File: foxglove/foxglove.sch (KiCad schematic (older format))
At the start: 87 parts, among them IC1 LFE5U-12F-6BG256C, J1 NEIGHBOR1, J2 NEIGHBOR2, J3 Conn_02x05_Odd_Even, J4 Conn_02x05_Odd_Even, J5 Conn_01x02_Female, J6 Conn_02x03_Odd_Even, J7 BONUS_ROW, U1 LM393, U2 ADP225, U25 74LVC1G53, U3 AP2127, U4 74LVC1G3157, U5 AP2127, U6 AP2127, U7 DAC084S085

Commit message: Routed ADC/DAC and FPGA passives
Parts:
- removed C17: 100nF, gsg-modules:0402, symbol Device:C
- removed C20: 10nF, gsg-modules:0402, symbol Device:C
- added TP1, TP2: TestPoint, gsg-modules:TESTPOINT-50MIL, symbol Connector:TestPoint
- U2: footprint Package_CSP:LFCSP-8_2x2mm_P0.5mm -> gsg-modules:SON50P200X200X60-9N
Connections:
- net +1V1: now also U2.7 (VOUT1), TP2.1
- net +2V5: now also U2.5 (VOUT2), TP1.1
- net +5V: now also U2.1 (EN1), U2.2 (EN2), U2.6 (VIN)
- net CSSPIN: now also J1.24 (Pin_24)
- net GND: now also U2.0 (EPAD)
- net VCC: no longer IC1.F6 (VCCIO0_1), IC1.F7 (VCCIO0_2)
- net at U2.4 (ADJ2): now also R41.1, R42.2
- net at U2.8 (ADJ1): now also R43.2, R44.1
- net J1.24: no longer names the net of IC1.R7 (PB6A)
- net J1.24: no longer J1.24 (Pin_24)
- new net VCCIO0: IC1.F6 (VCCIO0_1), IC1.F7 (VCCIO0_2)
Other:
- moved on the sheet: R41, R42, U2
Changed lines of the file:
@@
 Text Label -11900 8300 1    50   ~ 0
 J1.22
-Text Label -11800 8300 1    50   ~ 0
-J1.24
 Text Label -11700 8300 1    50   ~ 0
 J1.26
@@
 L gsg-symbols:ADP225 U2
 U 1 1 5CCD2B79
-P 10300 1600
-F 0 "U2" H 10275 1975 50  0000 C CNN
-F 1 "ADP225" H 10275 1884 50  0000 C CNN
-F 2 "Package_CSP:LFCSP-8_2x2mm_P0.5mm" H 10150 1600 50  0001 C CNN
-F 3 "" H 10150 1600 50  0001 C CNN
-F 4 "Analog Devices Inc. " H 10300 1600 50  0001 C CNN "Manufacturer"
-F 5 "ADP225ACPZ-R7" H 10300 1600 50  0001 C CNN "Part Number"
-F 6 "IC REG LINEAR POS ADJ 8LFCSP" H 10300 1600 50  0001 C CNN "Description"
-	1    10300 1600
+P 10200 1600
+F 0 "U2" H 10175 1975 50  0000 C CNN
+F 1 "ADP225" H 10175 1884 50  0000 C CNN
+F 2 "gsg-modules:SON50P200X200X60-9N" H 10050 1600 50  0001 C CNN
+F 3 "" H 10050 1600 50  0001 C CNN
+F 4 "Analog Devices Inc. " H 10200 1600 50  0001 C CNN "Manufacturer"
+F 5 "ADP225ACPZ-R7" H 10200 1600 50  0001 C CNN "Part Number"
+F 6 "IC REG LINEAR POS ADJ 8LFCSP" H 10200 1600 50  0001 C CNN "Description"
+	1    10200 1600
 	1    0    0    -1
 $EndComp
@@
 L power:GND #PWR0200
 U 1 1 5CD3745C
-P 9850 1650
-F 0 "#PWR0200" H 9850 1400 50  0001 C CNN
-F 1 "GND" H 9850 1500 50  0000 C CNN
-F 2 "" H 9850 1650 50  0001 C CNN
-F 3 "" H 9850 1650 50  0001 C CNN
-	1    9850 1650
+P 9700 1650
+F 0 "#PWR0200" H 9700 1400 50  0001 C CNN
+F 1 "GND" H 9700 1500 50  0000 C CNN
+F 2 "" H 9700 1650 50  0001 C CNN
+F 3 "" H 9700 1650 50  0001 C CNN
+	1    9700 1650
 	0    1    1    0
 $EndComp
 Wire Wire Line
-	9850 1650 9900 1650
-Wire Wire Line
 	10650 1650 11150 1650
 Wire Wire Line
@@
 L Device:R R42
 U 1 1 5CF1DBFB
-P 10250 1900
-F 0 "R42" V 10457 1900 50  0000 C CNN
-F 1 "100k" V 10366 1900 50  0000 C CNN
-F 2 "gsg-modules:0402" V 10180 1900 50  0001 C CNN
-F 3 "~" H 10250 1900 50  0001 C CNN
-	1    10250 1900
+P 10250 2000
+F 0 "R42" V 10457 2000 50  0000 C CNN
+F 1 "100k" V 10366 2000 50  0000 C CNN
+F 2 "gsg-modules:0402" V 10180 2000 50  0001 C CNN
+F 3 "~" H 10250 2000 50  0001 C CNN
+	1    10250 2000
 	0    1    1    0
 $EndComp
 Wire Wire Line
-	9900 1750 9900 1900
-Wire Wire Line
-	9900 1900 10100 1900
-Wire Wire Line
 	10650 1750 10700 1750
-Wire Wire Line
-	10400 1900 10700 1900
-Wire Wire Line
-	10700 1900 10700 1750
 $Comp
 L power:+2V5 #PWR0205
@@
 L Device:R R41
 U 1 1 5CFF97C1
-P 9700 1900
-F 0 "R41" V 9907 1900 50  0000 C CNN
-F 1 "25k" V 9816 1900 50  0000 C CNN
-F 2 "gsg-modules:0402" V 9630 1900 50  0001 C CNN
-F 3 "~" H 9700 1900 50  0001 C CNN
-	1    9700 1900
+P 9550 1900
+F 0 "R41" V 9757 1900 50  0000 C CNN
+F 1 "25k" V 9666 1900 50  0000 C CNN
+F 2 "gsg-modules:0402" V 9480 1900 50  0001 C CNN
+F 3 "~" H 9550 1900 50  0001 C CNN
+	1    9550 1900
 	0    1    1    0
 $EndComp
-Wire Wire Line
-	9850 1900 9900 1900
-Connection ~ 9900 1900
 $Comp
 L power:GND #PWR0207
 U 1 1 5D01F043
-P 9500 1900
-F 0 "#PWR0207" H 9500 1650 50  0001 C CNN
-F 1 "GND" H 9500 1750 50  0000 C CNN
-F 2 "" H 9500 1900 50  0001 C CNN
-F 3 "" H 9500 1900 50  0001 C CNN
-	1    9500 1900
+P 9350 1900
+F 0 "#PWR0207" H 9350 1650 50  0001 C CNN
+F 1 "GND" H 9350 1750 50  0000 C CNN
+F 2 "" H 9350 1900 50  0001 C CNN
+F 3 "" H 9350 1900 50  0001 C CNN
+	1    9350 1900
 	0    1    1    0
 $EndComp
 Wire Wire Line
-	9500 1900 9550 1900
-Wire Wire Line
-	9900 1550 9900 1500
-Wire Wire Line
-	9900 1500 9850 1500
-Connection ~ 9900 1500
-Wire Wire Line
-	9900 1500 9900 1450
+	9350 1900 9400 1900
 $Comp
 L power:+5V #PWR0208
 U 1 1 5D091620
-P 9850 1500
-F 0 "#PWR0208" H 9850 1350 50  0001 C CNN
-F 1 "+5V" H 9865 1673 50  0000 C CNN
-F 2 "" H 9850 1500 50  0001 C CNN
-F 3 "" H 9850 1500 50  0001 C CNN
-	1    9850 1500
+P 9700 1500
+F 0 "#PWR0208" H 9700 1350 50  0001 C CNN
+F 1 "+5V" H 9715 1673 50  0000 C CNN
+F 2 "" H 9700 1500 50  0001 C CNN
+F 3 "" H 9700 1500 50  0001 C CNN
+	1    9700 1500
 	0    -1   -1   0
 $EndComp
@@
 Text Label -10650 6200 3    50   ~ 0
 J1.14
-Text Label -11250 6200 3    50   ~ 0
-J1.24
 Text Label -10650 4700 1    50   ~ 0
 B2
@@
 Wire Wire Line
 	-13250 4700 -13250 4650
-Text Label -11950 1150 2    50   ~ 0
-VCCIO0
-$Comp
-L power:VCC #PWR033
-U 1 1 5D044ACD
-P -11750 1100
-F 0 "#PWR033" H -11750 950 50  0001 C CNN
-F 1 "VCC" H -11733 1273 50  0000 C CNN
-F 2 "" H -11750 1100 50  0001 C CNN
-F 3 "" H -11750 1100 50  0001 C CNN
-	1    -11750 1100
-	1    0    0    -1
-$EndComp
-$Comp
-L Device:C C20
-U 1 1 5D044BC6
-P -11750 1300
-F 0 "C20" H -11635 1346 50  0000 L CNN
-F 1 "10nF" H -11635 1255 50  0000 L CNN
-F 2 "gsg-modules:0402" H -11712 1150 50  0001 C CNN
-F 3 "~" H -11750 1300 50  0001 C CNN
-F 4 "Samsung Electro-Mechanics" H -11750 1300 50  0001 C CNN "Manufacturer"
-F 5 "CL05B103KO5NNNC " H -11750 1300 50  0001 C CNN "Part Number"
-F 6 "CAP CER 10000PF 16V X7R 0402 " H -11750 1300 50  0001 C CNN "Description"
-	1    -11750 1300
-	1    0    0    -1
-$EndComp
-$Comp
-L Device:C C17
-U 1 1 5D044C76
-P -12200 1300
-F 0 "C17" H -12085 1346 50  0000 L CNN
-F 1 "100nF" H -12085 1255 50  0000 L CNN
-F 2 "gsg-modules:0402" H -12162 1150 50  0001 C CNN
-F 3 "~" H -12200 1300 50  0001 C CNN
-F 4 "Taiyo Yuden " H -12200 1300 50  0001 C CNN "Manufacturer"
-F 5 "EMK105BJ104KV-F" H -12200 1300 50  0001 C CNN "Part Number"
-F 6 "CAP CER 0.1UF 16V X5R 0402" H -12200 1300 50  0001 C CNN "Description"
-	1    -12200 1300
-	1    0    0    -1
-$EndComp
-Wire Wire Line
-	-11750 1450 -11750 1500
-Connection ~ -11750 1450
-$Comp
-L power:GND #PWR034
-U 1 1 5D097A68
-P -11750 1500
-F 0 "#PWR034" H -11750 1250 50  0001 C CNN
-F 1 "GND" H -11745 1327 50  0000 C CNN
-F 2 "" H -11750 1500 50  0001 C CNN
-F 3 "" H -11750 1500 50  0001 C CNN
-	1    -11750 1500
-	1    0    0    -1
-$EndComp
-Wire Wire Line
-	-11750 1150 -11750 1100
-Connection ~ -11750 1150
-Wire Wire Line
-	-12200 1450 -11750 1450
-Wire Wire Line
-	-12200 1150 -11750 1150
 Text Label -11100 1150 2    50   ~ 0
 VCCIO1
@@
 Wire Wire Line
 	-9650 1450 -10050 1450
+Connection ~ -9650 1450
+Wire Wire Line
+	9700 1900 9750 1900
+Wire Wire Line
+	9750 1750 9750 1900
+Wire Wire Line
+	9700 1650 9750 1650
+Wire Wire Line
+	9700 1500 9750 1500
+Wire Wire Line
+	9750 1500 9750 1550
+Wire Wire Line
+	9750 1500 9750 1450
+Connection ~ 9750 1500
+Wire Wire Line
+	10700 2000 10400 2000
+Wire Wire Line
+	10700 1750 10700 2000
+Wire Wire Line
+	10100 2000 9750 2000
+Wire Wire Line
+	9750 2000 9750 1900
+Connection ~ 9750 1900
+Wire Wire Line
+	10150 1900 10100 1900
+$Comp
+L power:GND #PWR0109
+U 1 1 5D0B32F3
+P 10100 1900
+F 0 "#PWR0109" H 10100 1650 50  0001 C CNN
+F 1 "GND" H 10100 1750 50  0000 C CNN
+F 2 "" H 10100 1900 50  0001 C CNN
+F 3 "" H 10100 1900 50  0001 C CNN
+	1    10100 1900
+	0    1    1    0
+$EndComp
+$Comp
+L Connector:TestPoint TP2
+U 1 1 5D0B58A7
+P 12700 1350
+F 0 "TP2" H 12758 1470 50  0000 L CNN
+F 1 "TestPoint" H 12758 1379 50  0000 L CNN
+F 2 "gsg-modules:TESTPOINT-50MIL" H 12900 1350 50  0001 C CNN
+F 3 "~" H 12900 1350 50  0001 C CNN
+	1    12700 1350
+	1    0    0    -1
+$EndComp
+$Comp
+L Connector:TestPoint TP1
+U 1 1 5D0B5E51
+P 12250 1350
+F 0 "TP1" H 12308 1470 50  0000 L CNN
+F 1 "TestPoint" H 12308 1379 50  0000 L CNN
+F 2 "gsg-modules:TESTPOINT-50MIL" H 12450 1350 50  0001 C CNN
+F 3 "~" H 12450 1350 50  0001 C CNN
+	1    12250 1350
+	1    0    0    -1
+$EndComp
+$Comp
+L power:+1V1 #PWR0110
+U 1 1 5D0B608C
+P 12700 1400
+F 0 "#PWR0110" H 12700 1250 50  0001 C CNN
+F 1 "+1V1" H 12715 1573 50  0000 C CNN
+F 2 "" H 12700 1400 50  0001 C CNN
+F 3 "" H 12700 1400 50  0001 C CNN
+	1    12700 1400
+	-1   0    0    1
+$EndComp
+Wire Wire Line
+	12700 1400 12700 1350
+Wire Wire Line
+	12250 1400 12250 1350
+$Comp
+L power:+2V5 #PWR0113
+U 1 1 5D11AC1C
+P 12250 1400
+F 0 "#PWR0113" H 12250 1250 50  0001 C CNN
+F 1 "+2V5" H 12265 1573 50  0000 C CNN
+F 2 "" H 12250 1400 50  0001 C CNN
+F 3 "" H 12250 1400 50  0001 C CNN
+	1    12250 1400
+	-1   0    0    1
+$EndComp
 Wire Bus Line
 	-5400 2700 -3400 2700
@@
 Wire Bus Line
 	-2150 4150 -400 4150
-Connection ~ -9650 1450
+Text Label -11800 8300 1    50   ~ 0
+CSSPIN
 $EndSCHEMATC

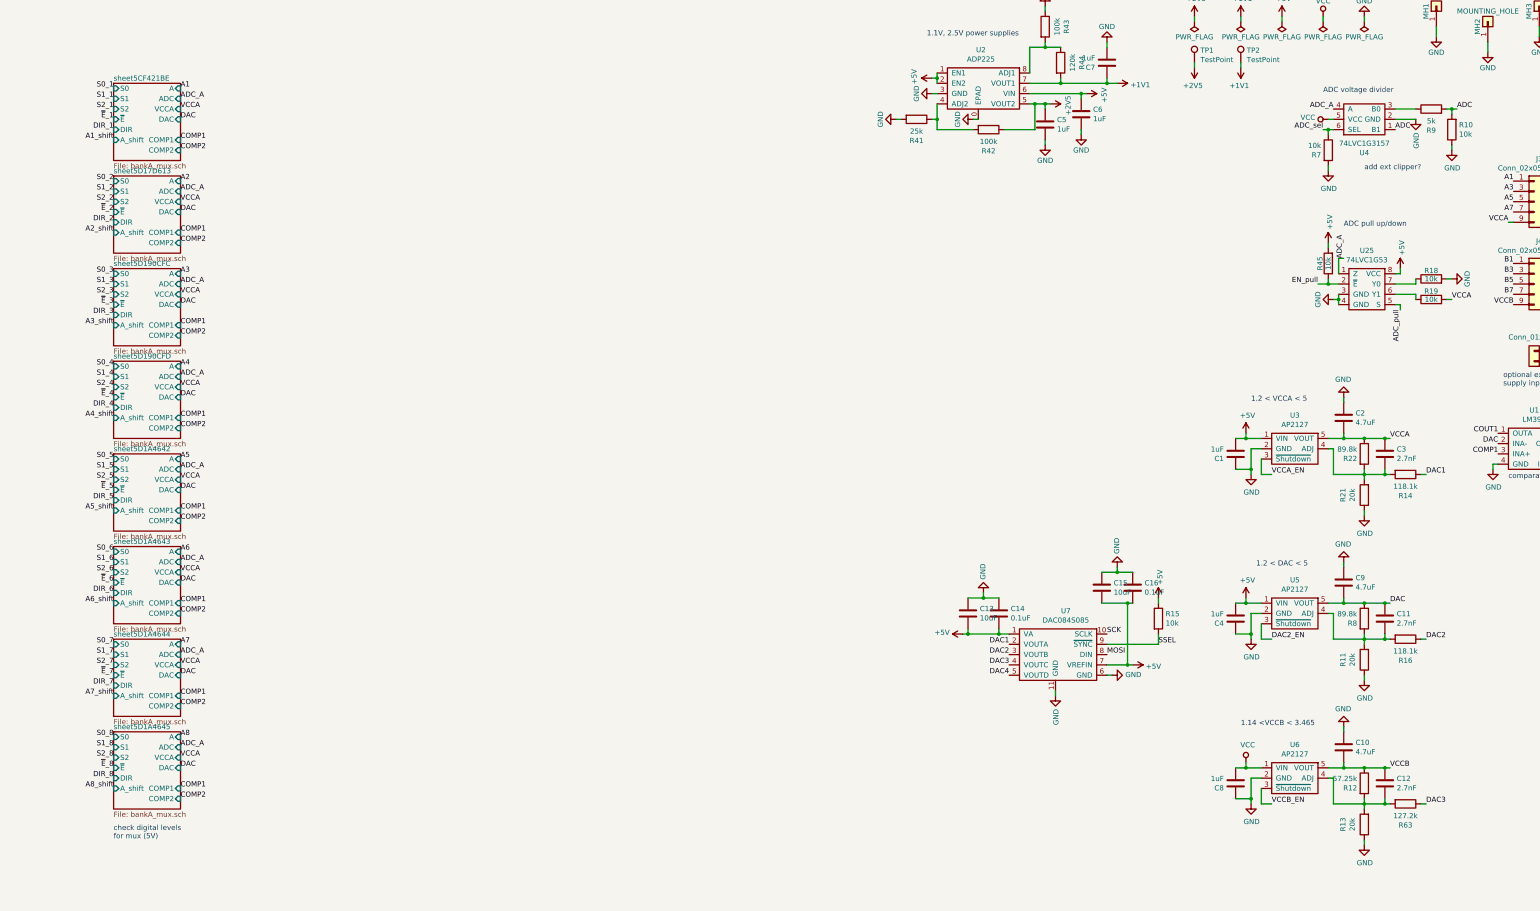
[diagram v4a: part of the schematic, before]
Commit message: Corrected DAC caps, added DAC test points
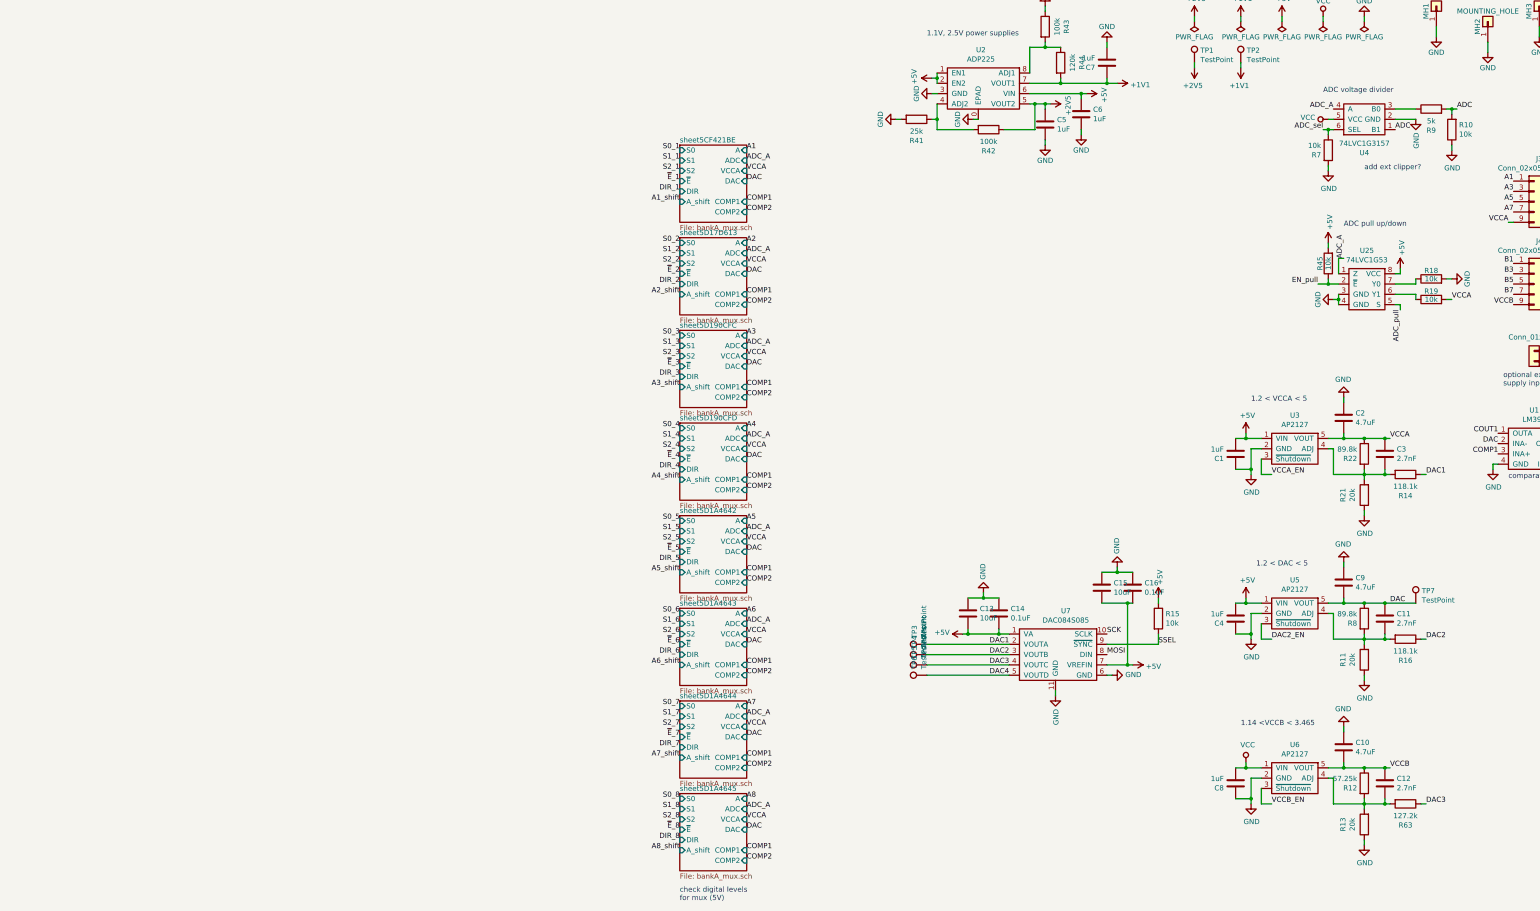
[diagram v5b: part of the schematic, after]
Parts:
- added TP3, TP4, TP5, TP6, TP7: TestPoint, gsg-modules:TESTPOINT-50MIL, symbol Connector:TestPoint
- C13, C15: footprint Capacitor_SMD:C_1206_3216Metric -> gsg-modules:0603; Description CAP TANT 10UF 10% 10V 1206 -> CAP TANT 10UF 20% 10V 0603; Part Number TAJA106K010TNJ -> F981A106MMA
- C14, C16: footprint gsg-modules:0805 -> gsg-modules:0402; Description CAP CER 0.1UF 25V X7R 0508 -> CAP CER 0.1UF 16V X5R 0402; Manufacturer Murata Electronics North America -> Taiyo Yuden; Part Number LLL216R71E104MA01L -> EMK105BJ104KV-F
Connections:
- net DAC: now also TP7.1
- net DAC1: now also TP3.1
- net DAC2: now also TP4.1
- net DAC3: now also TP5.1
- net DAC4: now also TP6.1
